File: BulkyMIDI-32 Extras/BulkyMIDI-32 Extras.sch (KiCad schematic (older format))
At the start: 43 parts, among them J1 DC IN, J10 MIDI2, J11 MIDI3, J2 MIDI OUT, J3 MIDI IN, J4 Conn_Extras, J5 MIDI1, J6 RS232 Module, J7 INPUT1, J8 INPUT2, J9 OUTPUT, M1 Mounting, M2 Mounting, M3 Mounting, M4 Mounting, U1 74HCT14

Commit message: Added vertical rotary encoder option
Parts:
- ENC1: value KY-040 -> Rotary Encoder; footprint Connector_PinHeader_2.54mm:PinHeader_1x05_P2.54mm_Horizontal -> BulkyMIDI-32:Vertical_Rotary_Encoder; symbol BulkyMIDI:KY-040 -> BulkyMIDI:Vertical_Rotary_Encoder
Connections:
- wire segments 145 -> 148
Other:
- note added: "4-pin connector for connecting up a rotary encoder, but\nbecause I couldn't find a pre-made module that would\nfit this is included as a separate PCB. This would have\nbeen easier if the real right-angle encoders weren't so\nexpensive."
- note removed: "5-pin connector for connecting up a rotary encoder such\nas the KY-040, note that we'll still need the SYNTH/ROM\nbuttons from the "simple_buttons" control scheme as\nwell."
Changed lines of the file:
@@
 RS-232 or TTL Serial USB adapter (optional)
 $Comp
-L BulkyMIDI:KY-040 ENC1
+L BulkyMIDI:Vertical_Rotary_Encoder ENC1
 U 1 1 62EDD8FE
-P 10050 7075
-F 0 "ENC1" H 9750 7500 50  0000 L CNN
-F 1 "KY-040" H 9750 7425 50  0000 L CNN
-F 2 "Connector_PinHeader_2.54mm:PinHeader_1x05_P2.54mm_Horizontal" H 10200 6965 50  0001 C CNN
-F 3 "~" H 10050 6865 50  0001 C CNN
-	1    10050 7075
-	1    0    0    -1
-$EndComp
-Text GLabel 9950 7650 3    50   Output ~ 0
+P 10050 6900
+F 0 "ENC1" H 9750 7325 50  0000 L CNN
+F 1 "Rotary Encoder" H 9750 7250 50  0000 L CNN
+F 2 "BulkyMIDI-32:Vertical_Rotary_Encoder" H 10200 6790 50  0001 C CNN
+F 3 "~" H 10050 6690 50  0001 C CNN
+	1    10050 6900
+	1    0    0    -1
+$EndComp
+Text GLabel 9900 7625 3    50   Output ~ 0
 SW_ENC
-$Comp
-L power:+3.3V #PWR02
-U 1 1 62F0DAFE
-P 10300 6675
-F 0 "#PWR02" H 10300 6525 50  0001 C CNN
-F 1 "+3.3V" H 10315 6848 50  0000 C CNN
-F 2 "" H 10300 6675 50  0001 C CNN
-F 3 "" H 10300 6675 50  0001 C CNN
-	1    10300 6675
-	1    0    0    -1
-$EndComp
-Text GLabel 10050 7650 3    50   Output ~ 0
+Text GLabel 10200 7625 3    50   Output ~ 0
 SW_UP
-Text GLabel 10150 7650 3    50   Output ~ 0
+Text GLabel 10100 7625 3    50   Output ~ 0
 SW_DOWN
 $Comp
 L power:GND #PWR06
 U 1 1 62F29FB2
-P 10425 7450
-F 0 "#PWR06" H 10425 7200 50  0001 C CNN
-F 1 "GND" H 10425 7300 50  0000 C CNN
-F 2 "" H 10425 7450 50  0001 C CNN
-F 3 "" H 10425 7450 50  0001 C CNN
-	1    10425 7450
+P 10000 8075
+F 0 "#PWR06" H 10000 7825 50  0001 C CNN
+F 1 "GND" H 10000 7925 50  0000 C CNN
+F 2 "" H 10000 8075 50  0001 C CNN
+F 3 "" H 10000 8075 50  0001 C CNN
+	1    10000 8075
 	-1   0    0    -1
 $EndComp
-Wire Wire Line
-	10425 7450 10425 7125
 $Comp
 L Connector:DIN-5_180degree J3
@@
 Text Notes 1075 5450 0    50   ~ 0
 Power section
-Text Notes 8900 5800 0    50   ~ 0
-5-pin connector for connecting up a rotary encoder such\nas the KY-040, note that we'll still need the SYNTH/ROM\nbuttons from the "simple_buttons" control scheme as\nwell.
+Text Notes 8900 5875 0    50   ~ 0
+4-pin connector for connecting up a rotary encoder, but\nbecause I couldn't find a pre-made module that would\nfit this is included as a separate PCB. This would have\nbeen easier if the real right-angle encoders weren't so\nexpensive.
 $Comp
 L Device:R_POT_Dual RV1
@@
 Wire Notes Line
 	4700 1275 11175 1275
+Wire Wire Line
+	10100 7550 10100 7625
+Wire Wire Line
+	10200 7550 10200 7625
+Wire Wire Line
+	9900 7550 9900 7625
+Wire Wire Line
+	10000 7550 10000 8075
 $EndSCHEMATC

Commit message: Baud rate converter parts
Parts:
- added C2, C5: 100nF, Capacitor_THT:C_Disc_D4.7mm_W2.5mm_P5.00mm, symbol Device:C_Small
- added C3, C4: 10pF, Capacitor_THT:C_Disc_D4.7mm_W2.5mm_P5.00mm, symbol Device:C_Small
- added D3: 1N4148, Diode_THT:D_DO-35_SOD27_P7.62mm_Horizontal, symbol Device:D_Small
- added J12: SERIAL, Connector_PinHeader_2.54mm:PinHeader_1x06_P2.54mm_Vertical, symbol Connector_Generic:Conn_01x06
- added J13: ICSP, Connector_PinHeader_2.54mm:PinHeader_2x03_P2.54mm_Vertical, symbol Connector_Generic:Conn_02x03_Odd_Even
- added J14: BIN/ASCII, symbol Connector_Generic:Conn_02x01
- added J15: BAUD_RATE, symbol Connector_Generic:Conn_02x02_Odd_Even
- added J16: Stacked RS232 Module, Connector_PinHeader_2.54mm:PinHeader_1x04_P2.54mm_Vertical, symbol rs232_module:RS232_Module
- added R17: 10k, Resistor_THT:R_Axial_DIN0207_L6.3mm_D2.5mm_P10.16mm_Horizontal, symbol Device:R
- added R18: 220, Resistor_THT:R_Axial_DIN0207_L6.3mm_D2.5mm_P10.16mm_Horizontal, symbol Device:R
- added R19: 2k2, Resistor_THT:R_Axial_DIN0207_L6.3mm_D2.5mm_P10.16mm_Horizontal, symbol Device:R
- added SW1: RESET, Button_Switch_THT:SW_PUSH_6mm, symbol Switch:SW_Push
- added U2: ATMEGA328_MCU, Package_DIP:DIP-28_W7.62mm_Socket_LongPads, symbol atmega328_mcu:ATMEGA328_MCU
- added U3: 6N138, Package_DIP:DIP-8_W7.62mm_Socket_LongPads, symbol Isolator:6N138
- added Y1: 16Mhz, Crystal:Crystal_HC49-4H_Vertical, symbol Device:Crystal_Small
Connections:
- net +3V3: now also J16.1; no longer J6.1
- net +5V: now also J6.1, C2.2, J12.4 (Pin_4), J13.2 (Pin_2), R17.1, R19.1, U2.20 (AVCC), U2.21 (AREF), U2.7 (VCC), U3.8 (VCC)
- net GND: now also C2.1, C3.2, C4.2, J12.6 (Pin_6), J13.6 (Pin_6), J14.2 (Pin_2), J15.2 (Pin_2), J15.4 (Pin_4), J16.4, SW1.1, U2.22 (GND), U2.8 (GND), U3.5 (GND); no longer U1.11, U1.13
- net MIDI_OUT: now also R1.2, U2.28 ((PCINT13/SCL/ADC5)PC5)
- net RX_TTL: now also J16.2; no longer J6.2
- net TX_TTL: now also J16.3; no longer J6.3
- net at J3.4: now also R18.2
- net at J3.5: now also D3.2 (A), U3.3 (C2)
- net at U1.10: now also U1.13
- net MIDI_IN: now reaches U1.12
- net MIDI_IN: now also U2.27 ((PCINT12/SDA/ADC4)PC4)
- new net: C5.1, J12.1 (Pin_1)
- new net: J14.1 (Pin_1), U2.11 ((PCINT21/OC0B/T1)PD5)
- new net: J15.1 (Pin_1), U2.12 ((PCINT22/OC0A/AIN0)PD6)
- new net: J15.3 (Pin_3), U2.13 ((PCINT23/AIN1)PD7)
- new net: J13.4 (Pin_4), U2.17 ((PCINT3/OC2A/MOSI)PB3)
- new net: J13.1 (Pin_1), U2.18 ((PCINT4/MISO)PB4)
- new net: J13.3 (Pin_3), U2.19 ((PCINT5/SCK)PB5)
- new net: D3.1 (K), R18.1, U3.2 (C1)
- new net: R19.2, U1.11, U3.6 (VO2)
- new net RS232_RxD: J12.3 (Pin_3), J6.2, U2.2 (RXD)
- new net RS232_TxD: J12.2 (Pin_2), J6.3, U2.3 (TXD)
- new net XTAL1: C3.1, U2.9 (XTAL1), Y1.1
- new net XTAL2: C4.1, U2.10 (XTAL2), Y1.2
- new net ~RESET: C5.2, J13.5 (Pin_5), R17.2, SW1.2, U2.1 (~RESET)
- no-connect marks 23 -> 30
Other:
- note added: "4-pin connector for connecting up a rotary encoder, but because I couldn't find a pre-made\nmodule that would fit this is included as a separate PCB. This would have been easier if the\nreal right-angle encoders weren't so expensive."
- note added: "RS-232 Baud rate converter"
- note removed: "4-pin connector for connecting up a rotary encoder, but\nbecause I couldn't find a pre-made module that would\nfit this is included as a separate PCB. This would have\nbeen easier if the real right-angle encoders weren't so\nexpensive."
- note removed: "NOT completed, the connectors are just here as physical placeholders"
- note removed: "RS-232 or TTL Serial USB adapter (optional)"
- moved on the sheet: C1, C6, D1, D2, ENC1, J1, J10, J11, J2, J3, J4, J5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

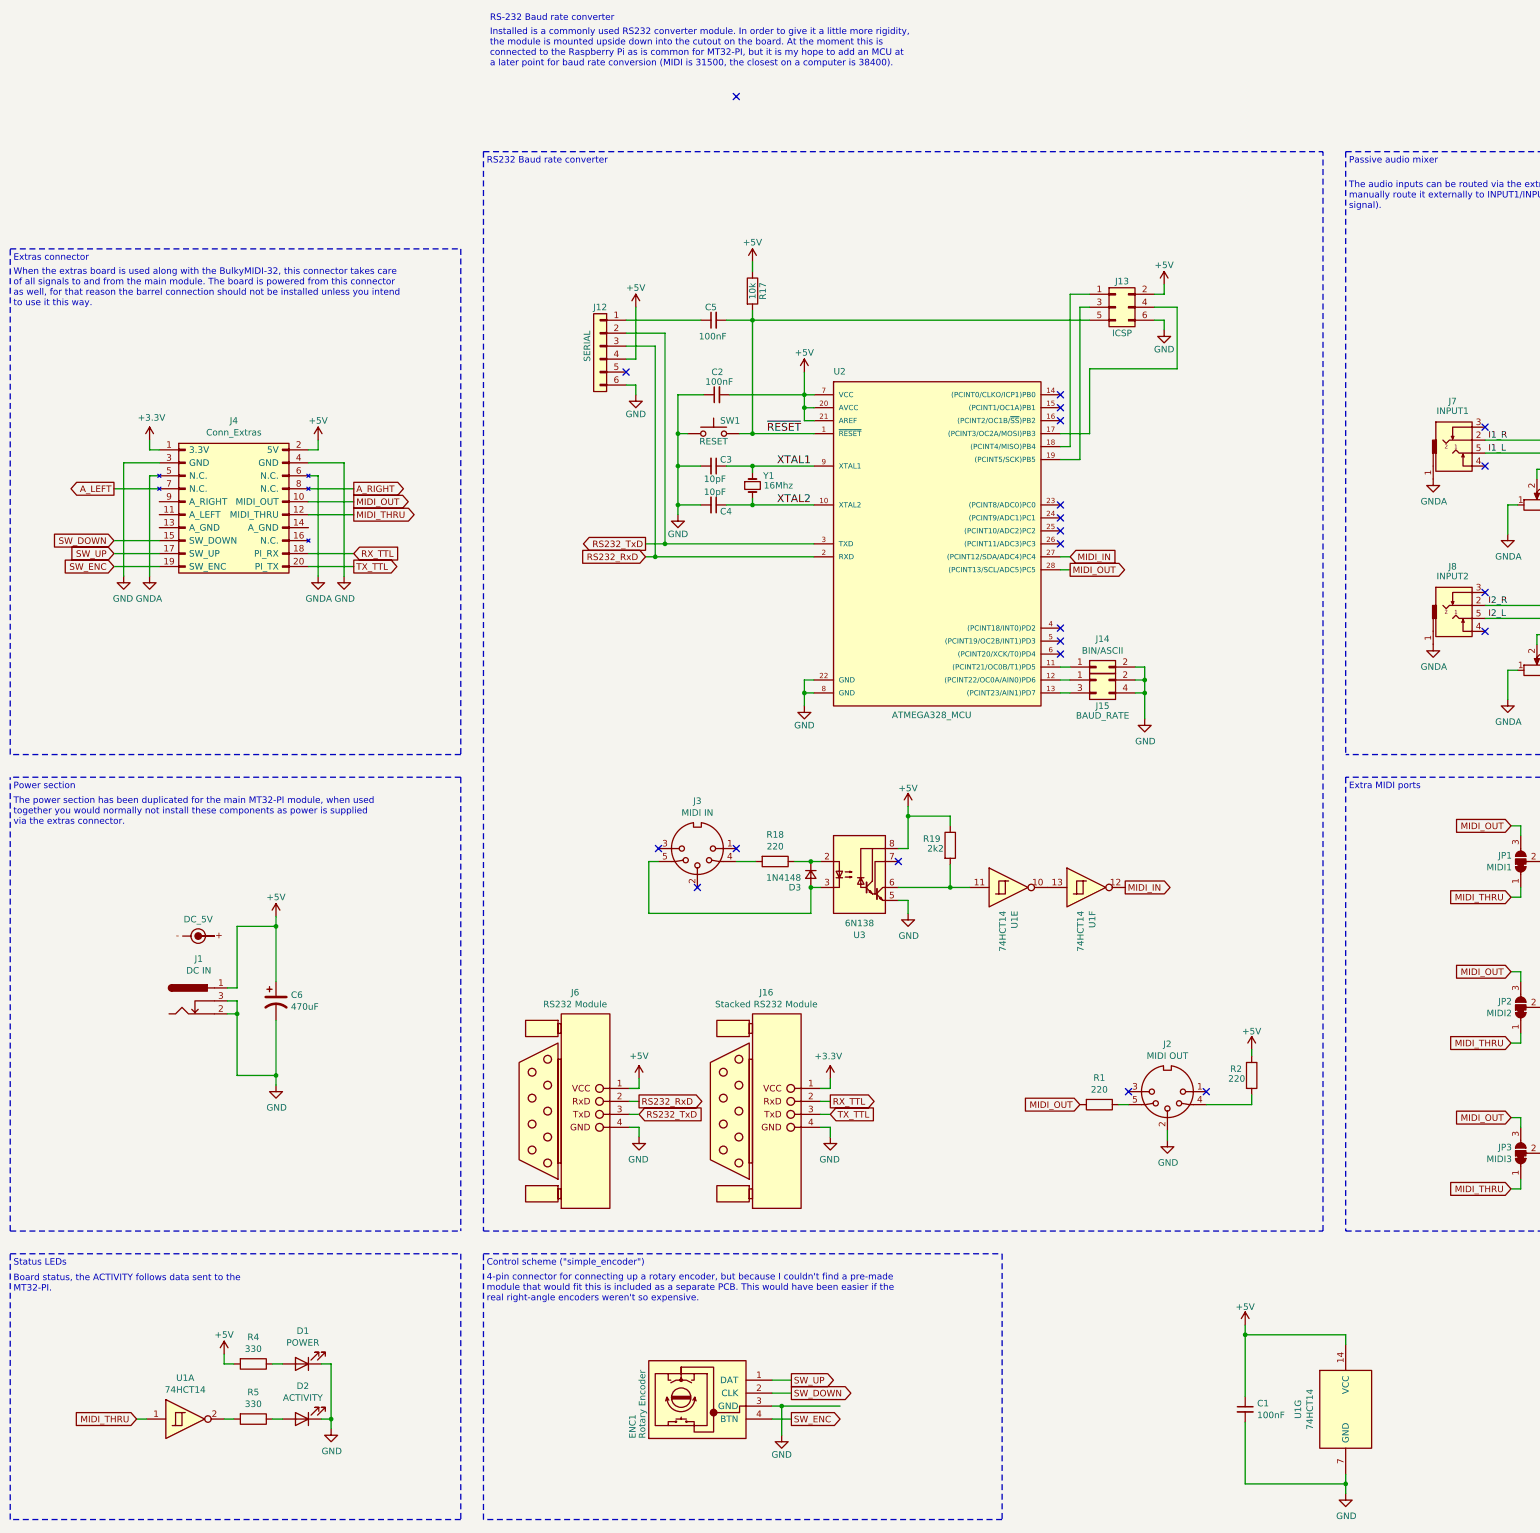
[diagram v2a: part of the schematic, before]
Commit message: Routed tracks for extras board
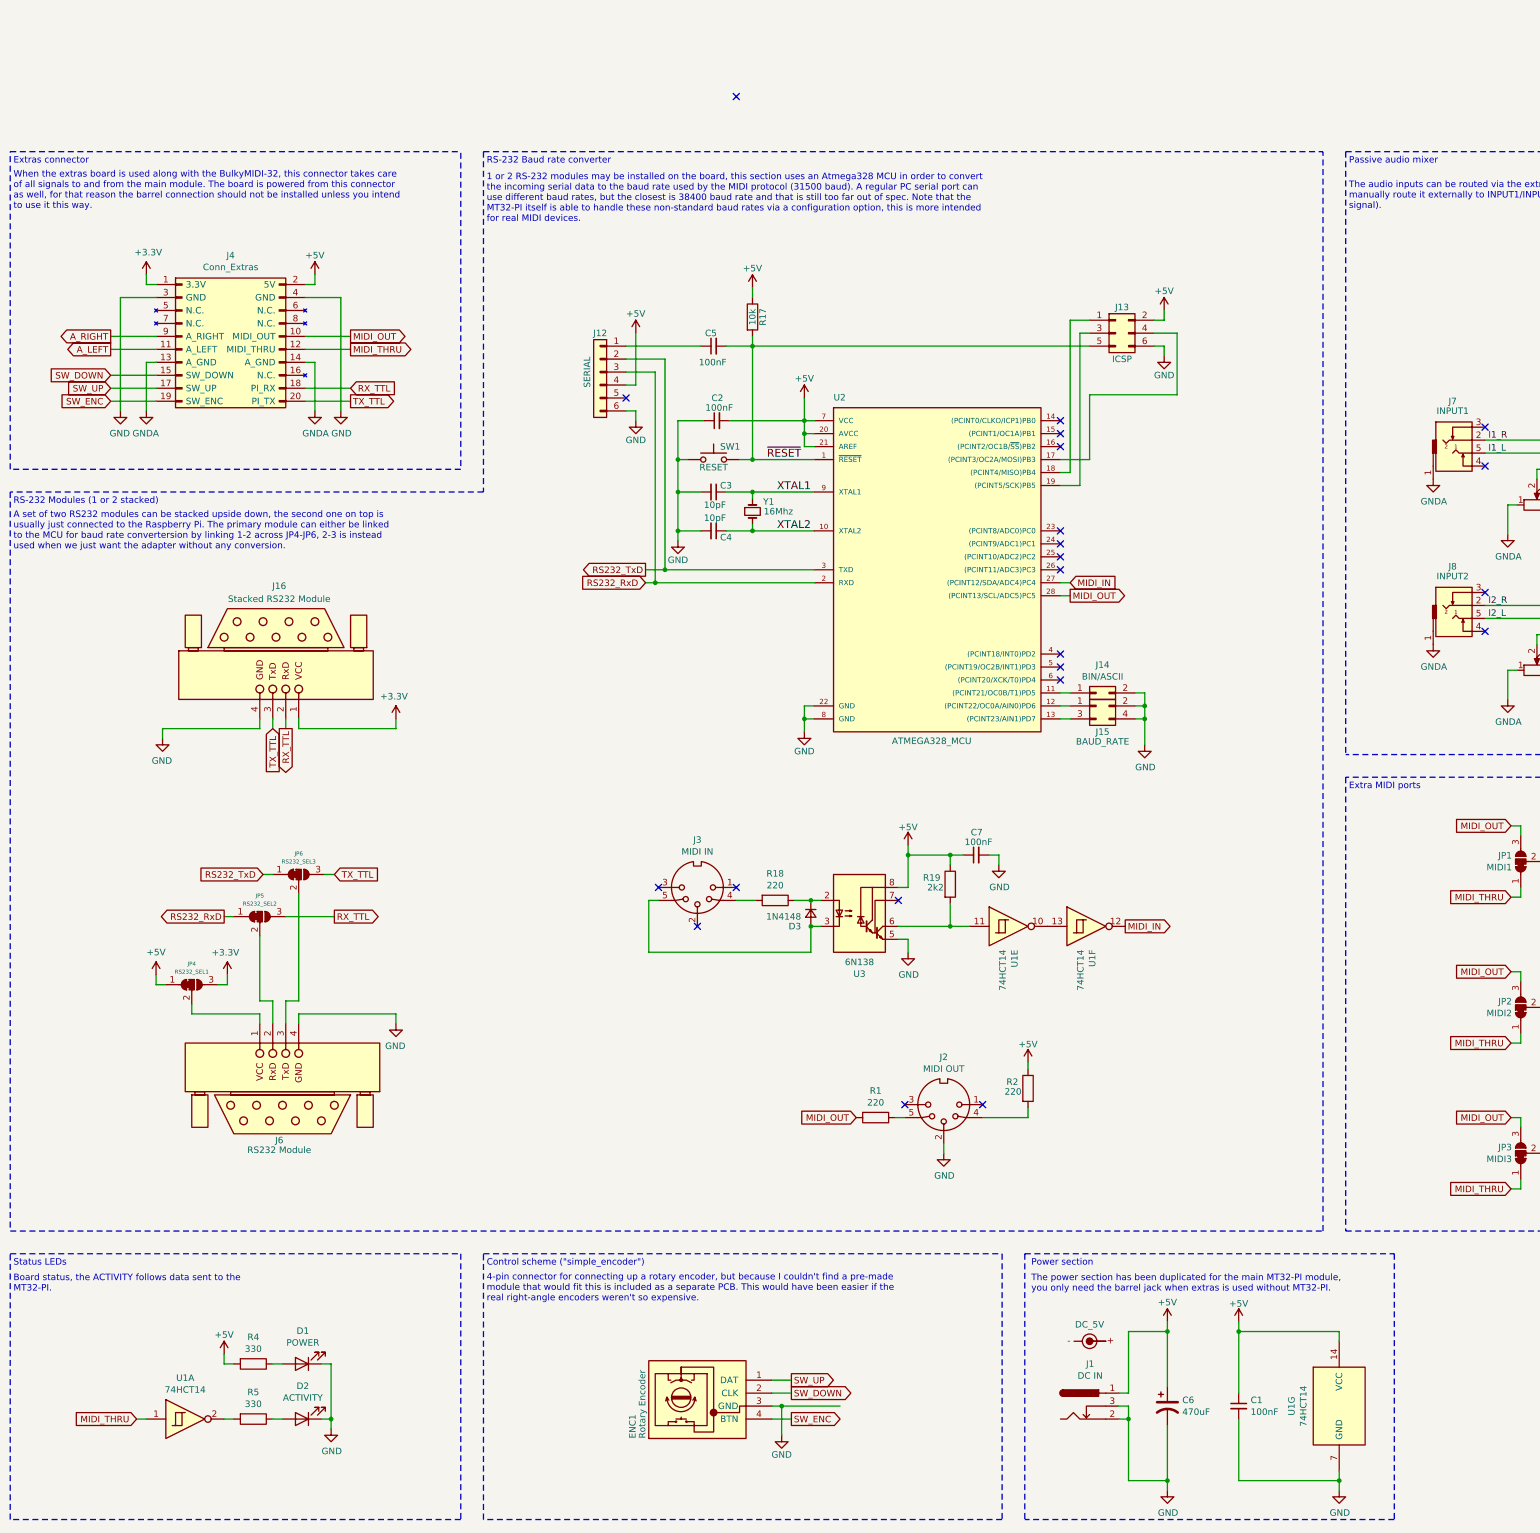
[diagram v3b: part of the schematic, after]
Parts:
- added C7: 100nF, Capacitor_THT:C_Disc_D4.7mm_W2.5mm_P5.00mm, symbol Device:C_Small
- added JP4: RS232_SEL1, Jumper:SolderJumper-3_P1.3mm_Open_RoundedPad1.0x1.5mm, symbol Jumper:SolderJumper_3_Bridged12
- added JP5: RS232_SEL2, Jumper:SolderJumper-3_P1.3mm_Open_RoundedPad1.0x1.5mm, symbol Jumper:SolderJumper_3_Bridged12
- added JP6: RS232_SEL3, Jumper:SolderJumper-3_P1.3mm_Open_RoundedPad1.0x1.5mm, symbol Jumper:SolderJumper_3_Bridged12
- J14: footprint (none) -> Connector_PinHeader_2.54mm:PinHeader_1x02_P2.54mm_Vertical
- J15: footprint (none) -> Connector_PinHeader_2.54mm:PinHeader_2x02_P2.54mm_Vertical
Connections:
- net +3V3: now also JP4.3 (B)
- net +5V: now also C7.1, JP4.1 (A); no longer J6.1
- net A_LEFT: now also J4.11 (A_LEFT); no longer J4.7 (N.C.)
- net A_RIGHT: now also J4.9 (A_RIGHT); no longer J4.8 (N.C.)
- net GND: now also C7.2
- net GNDA: now also J4.13 (A_GND), J4.14 (A_GND); no longer J4.5 (N.C.), J4.6 (N.C.)
- net RS232_RxD: now also JP5.1 (A); no longer J6.2
- net RS232_TxD: now also JP6.1 (A); no longer J6.3
- net RX_TTL: now also JP5.3 (B)
- net TX_TTL: now also JP6.3 (B)
- new net: J6.1, JP4.2 (C)
- new net: J6.2, JP5.2 (C)
- new net: J6.3, JP6.2 (C)
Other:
- note added: "1 or 2 RS-232 modules may be installed on the board, this section uses an Atmega328 MCU in order to convert\nthe incoming serial data to the baud rate used by the MIDI protocol (31500 baud). A regular PC serial port can\nuse different baud rates, but the closest is 38400 baud rate and that is still too far out of spec. Note that the\nMT32-PI itself is able to handle these non-standard baud rates 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"
- note added: "A set of two RS232 modules can be stacked upside down, the second one on top is\nusually just connected to the Raspberry Pi. The primary module can either be linked\nto the MCU for baud rate convertersion by linking 1-2 across JP4-JP6, 2-3 is instead\nused when we just want the adapter without any conversion."
- note added: "RS-232 Modules (1 or 2 stacked)"
- note added: "The power section has been duplicated for the main MT32-PI module,\nyou only need the barrel jack when extras is used without MT32-PI."
- note removed: "Installed is a commonly used RS232 converter module. In order to give it a little more rigidity,\nthe module is mounted upside down into the cutout on the board. At the moment this is\nconnected to the Raspberry Pi as is common for MT32-PI, but it is my hope to add an MCU at\na later point for baud rate conversion (MIDI is 31500, the closest on a computer is 38400)."
- note removed: "RS232 Baud rate converter"
- note removed: "The power section has been duplicated for the main MT32-PI module, when used\ntogether you would normally not install these components as power is supplied\nvia the extras connector."
- moved on the sheet: C1, C2, C3, C4, C5, C6, D3, J1, J12, J13, J14, J15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

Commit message: Fixed RX/TX swapped
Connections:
- net MIDI_OUT: no longer J4.10 (MIDI_OUT), JP1.3 (B), JP2.3 (B), JP3.3 (B)
- net at J6.2: now also JP6.2 (C); no longer JP5.2 (C)
- net at J6.3: now also JP5.2 (C); no longer JP6.2 (C)
- net MIDI_THRU renamed MIDI_THRUn
- net RS232_RxD renamed MCU_RX
- net RS232_TxD renamed MCU_TX
- net RX_TTL renamed PI_RX
- net PI_RX: now also J16.3; no longer J16.2
- net TX_TTL renamed PI_TX
- net PI_TX: now also J16.2; no longer J16.3
- new net MIDI_OUTn: J4.10 (MIDI_OUT), JP1.3 (B), JP2.3 (B), JP3.3 (B)
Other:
- note added: "DTR"
- note added: "GND"
- note added: "RxD"
- note added: "The audio inputs can be routed via the extras connector from the main module, alternatively you can\nmanually route it externally to INPUT1/INPUT2. The two inputs will passively be mixed into the output\nsound, note that the level will be slightly lower on the output as compared to directly from the DAC."
- note added: "TxD"
- note added: "USB-TTL Adapter"
- note added: "VCC"
- note removed: "The audio inputs can be routed via the extras connector from the main module, alternatively you can\nmanually route it externally to INPUT1/INPUT2 if you prefer (as this offers a way of controllng the\nsignal)."
- moved on the sheet: J7, J8, J9, JP5, JP6, R10, R11, R12, R7, R8, R9, RV1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
